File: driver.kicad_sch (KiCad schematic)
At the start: 26 parts, among them U10 74AUC2G32, U11 74AUC2G32, U12 74AUC2G32, U13 74AUC2G32, U14 74AUC2G32, U15 Inverter_Schmitt_Dual, U16 Inverter_Schmitt_Dual, U17 SN74AUP2G08, U18 SN74AUP2G08, U19 SN74AUP2G08, U20 SN74AUP2G08, U21 SN74AUP2G08, U22 74AUC2G32, U23 74AUC2G32, U24 74AUC2G32, U25 74AUC2G32, U26 74AUC2G32, U3 SN74AUP2G08, U4 SN74AUP2G08, U5 SN74AUP2G08, U6 SN74AUP2G08, U7 SN74AUP2G08, U8 SN74AUP2G08, U9 74AUC2G32

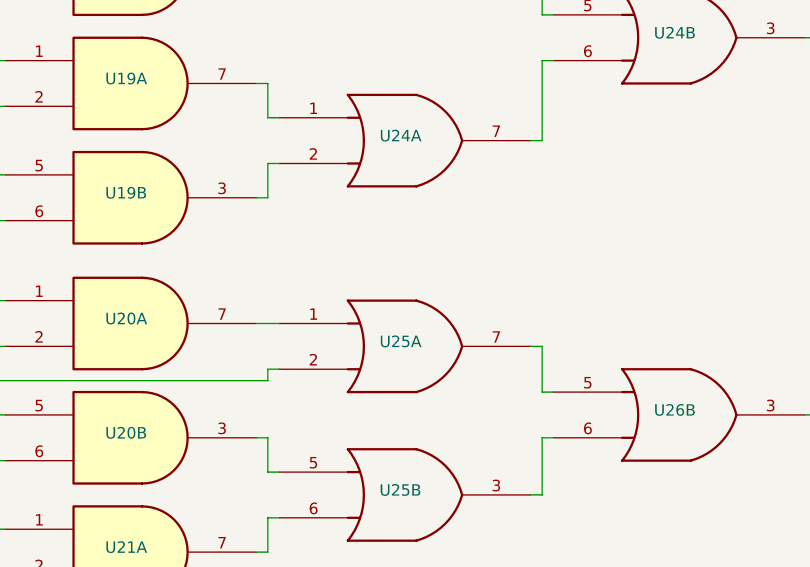
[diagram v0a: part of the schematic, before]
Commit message: pcb: add tooling holes and fiducials
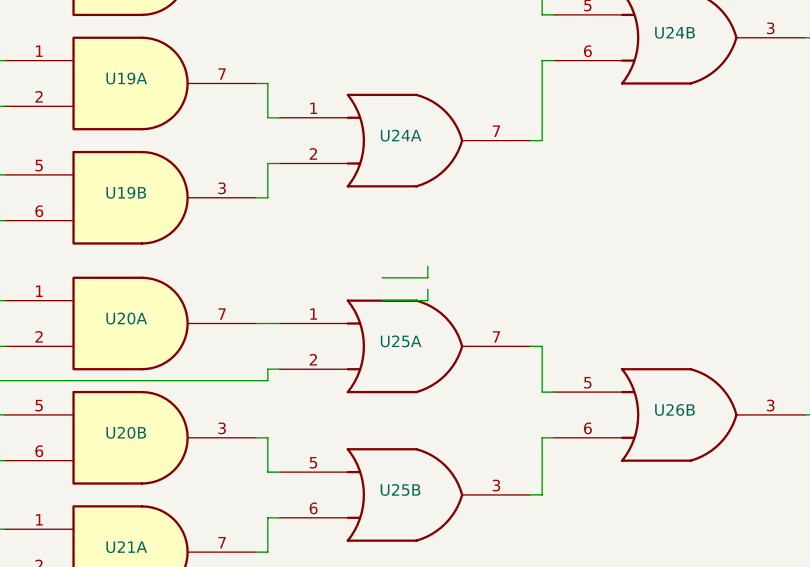
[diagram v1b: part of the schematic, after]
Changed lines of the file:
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@@
+	(wire
+		(pts
+			(xy 220.98 104.14) (xy 220.98 102.87)
+		)
+		(stroke
+			(width 0)
+			(type default)
+		)
+	)
 	(wire
 		(pts
@@
 	(wire
 		(pts
+			(xy 215.9 101.6) (xy 220.98 101.6)
+		)
+		(stroke
+			(width 0)
+			(type default)
+		)
+	)
+	(wire
+		(pts
 			(xy 83.82 25.4) (xy 85.09 25.4)
 		)
@@
 	(wire
 		(pts
+			(xy 215.9 104.14) (xy 220.98 104.14)
+		)
+		(stroke
+			(width 0)
+			(type default)
+		)
+	)
+	(wire
+		(pts
 			(xy 83.82 26.67) (xy 83.82 25.4)
 		)
@@
 		)
 		(stroke
+			(width 0)
+			(type default)
+		)
+	)
+	(wire
+		(pts
+			(xy 220.98 101.6) (xy 220.98 100.33)
+		)
+		(stroke

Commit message: pcb: route segments drivers
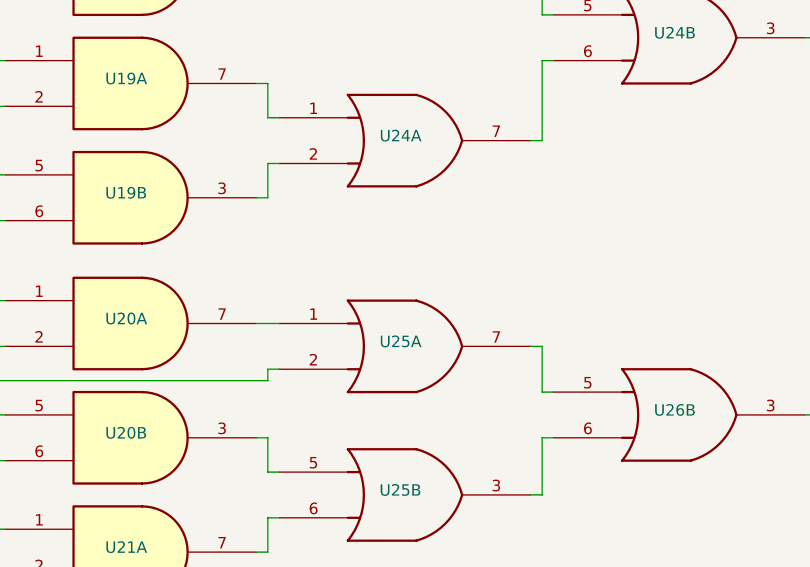
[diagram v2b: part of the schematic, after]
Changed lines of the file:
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@@
-	(wire
-		(pts
-			(xy 220.98 104.14) (xy 220.98 102.87)
-		)
-		(stroke
-			(width 0)
-			(type default)
-		)
-	)
 	(wire
 		(pts
@@
 	(wire
 		(pts
-			(xy 215.9 101.6) (xy 220.98 101.6)
-		)
-		(stroke
-			(width 0)
-			(type default)
-		)
-	)
-	(wire
-		(pts
 			(xy 83.82 25.4) (xy 85.09 25.4)
 		)
@@
 	(wire
 		(pts
-			(xy 215.9 104.14) (xy 220.98 104.14)
-		)
-		(stroke
-			(width 0)
-			(type default)
-		)
-	)
-	(wire
-		(pts
 			(xy 83.82 26.67) (xy 83.82 25.4)
 		)
@@
 		)
 		(stroke
-			(width 0)
-			(type default)
-		)
-	)
-	(wire
-		(pts
-			(xy 220.98 101.6) (xy 220.98 100.33)
-		)
-		(stroke
